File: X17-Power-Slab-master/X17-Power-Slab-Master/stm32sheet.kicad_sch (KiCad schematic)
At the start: 18 parts, among them J4 Conn_01x05, SW2 1825910-6, U4 STM32F091CCTx, U7 ABLS-8.000MHZ-B2-T

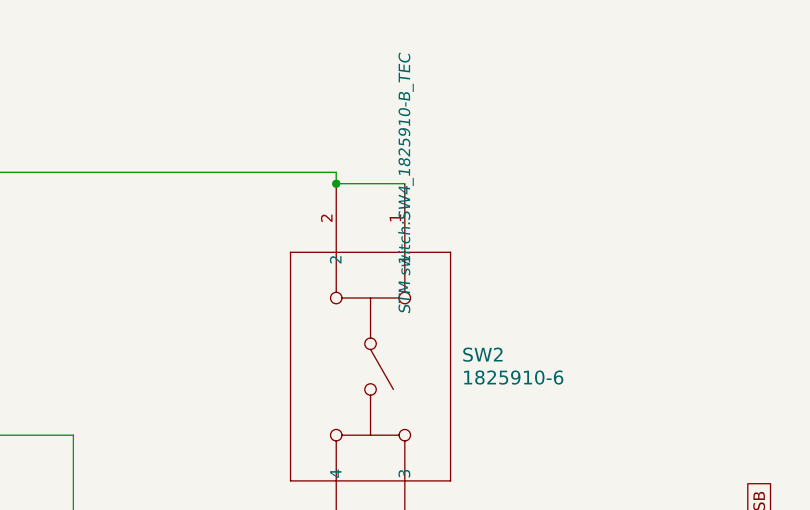
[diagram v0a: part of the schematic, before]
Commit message: Connector pins renamed and attempt @ fixing airwires for 5V Brick
Still don't understand why the airwire from 5V to 12V_5V_GND test point exists, I also now have airwires across all my P08_1 pins despite the same set up existing for 12V.
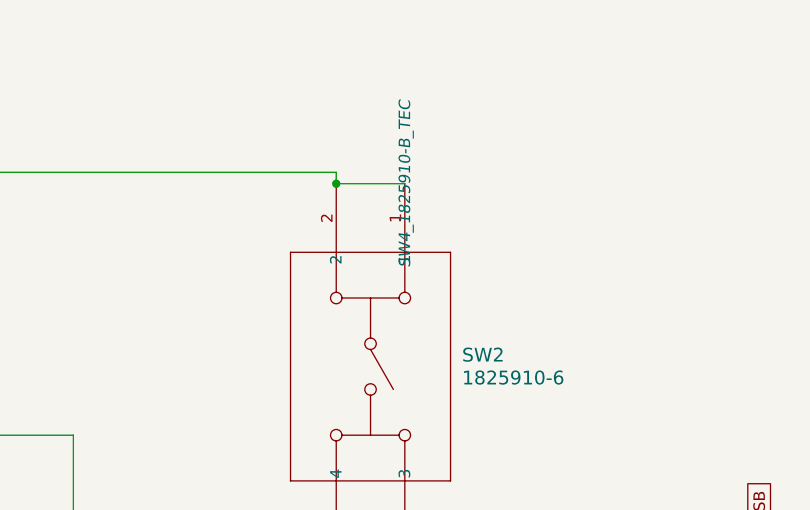
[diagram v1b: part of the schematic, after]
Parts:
- SW2: footprint STM switch:SW4_1825910-B_TEC -> SW4_1825910-B_TEC
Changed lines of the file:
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@@
 			)
 		)
-		(property "Footprint" "STM switch:SW4_1825910-B_TEC"
+		(property "Footprint" "SW4_1825910-B_TEC"
 			(at 81.28 58.42 0)
 			(effects

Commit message: Minor Edits
Some layout edits, got rid of stm, not done yet
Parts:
- removed C10, C11, C12, C13, C18: 0.1uF, Capacitor_SMD:C_0603_1608Metric_Pad1.08x0.95mm_HandSolder, symbol Device:C
- removed C14, C15: 4.7uF, Capacitor_SMD:C_0603_1608Metric_Pad1.08x0.95mm_HandSolder, symbol Device:C
- removed C16, C17: 18pF, Capacitor_SMD:C_0603_1608Metric_Pad1.08x0.95mm_HandSolder, symbol Device:C
- removed D3: LED, LED_SMD:LED_0805_2012Metric_Pad1.15x1.40mm_HandSolder, symbol Device:LED
- removed J4: Conn_01x05, Connector_PinHeader_2.54mm:PinHeader_1x05_P2.54mm_Vertical, symbol Connector_Generic:Conn_01x05
- removed R20: 470, Resistor_SMD:R_0603_1608Metric_Pad0.98x0.95mm_HandSolder, symbol Device:R_US
- removed R21, R22: 4.7k, Resistor_SMD:R_0603_1608Metric_Pad0.98x0.95mm_HandSolder, symbol Device:R_US
- removed R26: 10k, Resistor_SMD:R_0603_1608Metric_Pad0.98x0.95mm_HandSolder, symbol Device:R_US
- removed SW2: 1825910-6, SW4_1825910-B_TEC, symbol STM Switch Symbol:1825910-6
- removed U4: STM32F091CCTx, Package_QFP:LQFP-48_7x7mm_P0.5mm, symbol MCU_ST_STM32F0:STM32F091CCTx
- removed U7: ABLS-8.000MHZ-B2-T, footprints:ABLS-8.000MHZ-B2-T_ABR, symbol STM32_Oscillator:ABLS-8.000MHZ-B2-T
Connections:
- no-connect marks 21 -> 0
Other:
- note removed: "External Oscillator for STM32F0 8MHz ECS-2520MV-080-CN-TR"
- note removed: "NRST_PSB to other side"
- note removed: "STM Connector"
